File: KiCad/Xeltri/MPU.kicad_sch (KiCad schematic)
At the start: 1 part, among them U2 V851S

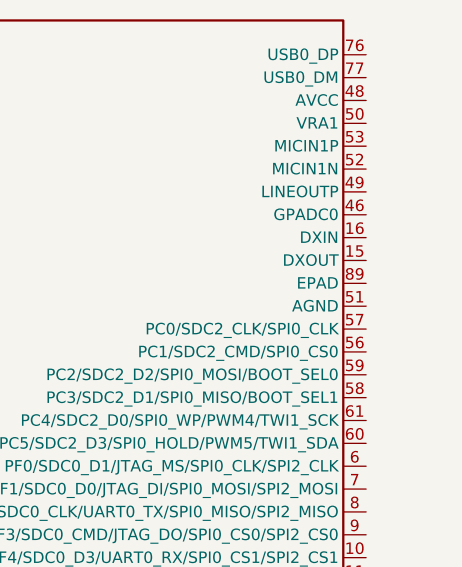
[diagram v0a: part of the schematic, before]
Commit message: Update KiCad project files: enhance .gitignore for sensitive data, refine component properties in schematics, and remove obsolete MCU configuration file. Added LCSC part numbers and datasheets for various components.
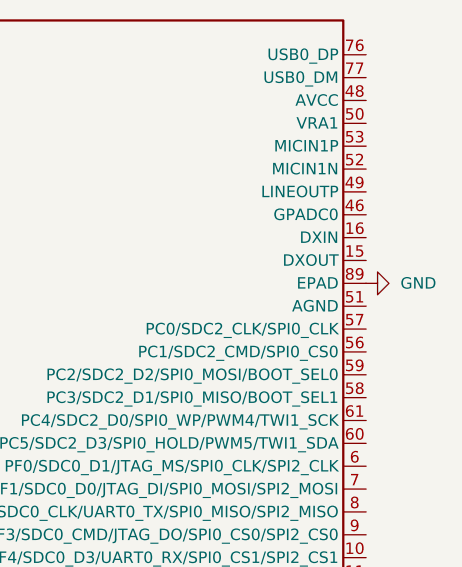
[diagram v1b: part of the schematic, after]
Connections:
- net GND: now reaches U2.89 (EPAD)
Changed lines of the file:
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@@
+		)
+	)
+	(symbol
+		(lib_id "power:GND")
+		(at 312.42 95.25 90)
+		(unit 1)
+		(exclude_from_sim no)
+		(in_bom yes)
+		(on_board yes)
+		(dnp no)
+		(fields_autoplaced yes)
+		(property "Reference" "#PWR0119"
+			(at 318.77 95.25 0)
+			(effects
+				(font
+					(size 1.27 1.27)
+				)
+				(hide yes)
+			)
+		)
+		(property "Value" "GND"
+			(at 316.23 95.2499 90)
+			(effects
+				(font
+					(size 1.27 1.27)
+				)
+				(justify right)
+			)
+		)
+		(property "Footprint" ""
+			(at 312.42 95.25 0)
+			(effects
+				(font
+					(size 1.27 1.27)
+				)
+				(hide yes)
+			)
+		)
+		(property "Datasheet" ""
+			(at 312.42 95.25 0)
+			(effects
+				(font
+					(size 1.27 1.27)
+				)
+				(hide yes)
+			)
+		)
+		(property "Description" "Power symbol creates a global label with name \"GND\" , ground"
+			(at 312.42 95.25 0)
+			(effects
+				(font
+					(size 1.27 1.27)
+				)
+				(hide yes)
+			)
+		)
+		(pin "1"
+		)
+		(instances
+			(project ""
+				(path "/b9ed8ff9-3a91-4311-b656-324fcf6f7e0c/7aec3465-79cd-4dd7-b3bd-c0d6af68e150"
+					(reference "#PWR0119")
+					(unit 1)
+				)
+			)
 		)
 	)
